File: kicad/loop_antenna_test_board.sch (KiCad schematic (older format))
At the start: 5 parts

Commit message: added board layout
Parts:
- C1, C2: footprint (none) -> loop_antenna_test_board:CAP
- C3: footprint (none) -> loop_antenna_test_board:CAP_TUNABLE
- R1: footprint (none) -> loop_antenna_test_board:RFM69W
- R2: footprint (none) -> loop_antenna_test_board:RFM69W_BB
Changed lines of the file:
@@
 LIBS:valves
 LIBS:loop_antenna_test_board
+LIBS:loop_antenna_test_board-cache
 EELAYER 25 0
 EELAYER END
@@
 F 0 "R1" H 5450 2250 60  0000 C CNN
 F 1 "RFM69W" H 5000 2950 60  0000 C CNN
-F 2 "" H 5050 3200 60  0000 C CNN
+F 2 "loop_antenna_test_board:RFM69W" H 5050 3200 60  0001 C CNN
 F 3 "" H 5050 3200 60  0000 C CNN
 	1    5000 2950
@@
 F 0 "R2" H 5450 4050 60  0000 C CNN
 F 1 "RFM69W_BB" H 5000 4750 60  0000 C CNN
-F 2 "" H 5050 5000 60  0000 C CNN
+F 2 "loop_antenna_test_board:RFM69W_BB" H 5050 5000 60  0001 C CNN
 F 3 "" H 5050 5000 60  0000 C CNN
 	1    5000 4750
@@
 F 0 "C1" H 7275 3600 50  0000 L CNN
 F 1 "C" H 7275 3400 50  0000 L CNN
-F 2 "" H 7288 3350 50  0000 C CNN
+F 2 "loop_antenna_test_board:CAP" H 7288 3350 50  0001 C CNN
 F 3 "" H 7250 3500 50  0000 C CNN
 	1    7250 3500
@@
 F 0 "C2" H 7275 4150 50  0000 L CNN
 F 1 "C" H 7275 3950 50  0000 L CNN
-F 2 "" H 7288 3900 50  0000 C CNN
+F 2 "loop_antenna_test_board:CAP" H 7288 3900 50  0001 C CNN
 F 3 "" H 7250 4050 50  0000 C CNN
 	1    7250 4050
@@
 F 0 "C3" H 7310 4520 50  0000 C CNN
 F 1 "CTRIM" H 7370 4460 50  0000 C CNN
-F 2 "" H 7250 4600 50  0000 C CNN
+F 2 "loop_antenna_test_board:CAP_TUNABLE" H 7250 4600 50  0001 C CNN
 F 3 "" H 7250 4600 50  0000 C CNN
 	1    7250 4600
@@
 	6950 3800 7250 3800
 Connection ~ 7250 3800
+Text Label 7550 3850 0    60   ~ 0
+ANTENNA
 $EndSCHEMATC

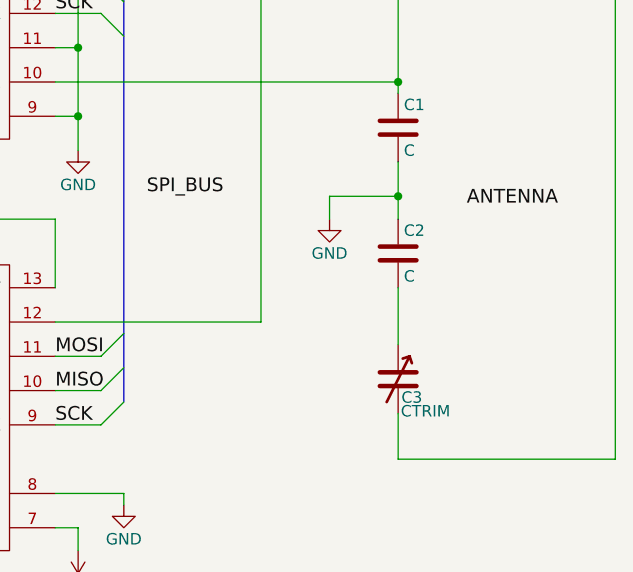
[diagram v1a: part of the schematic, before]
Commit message: switched to only having two positions for capacitors in the antenna
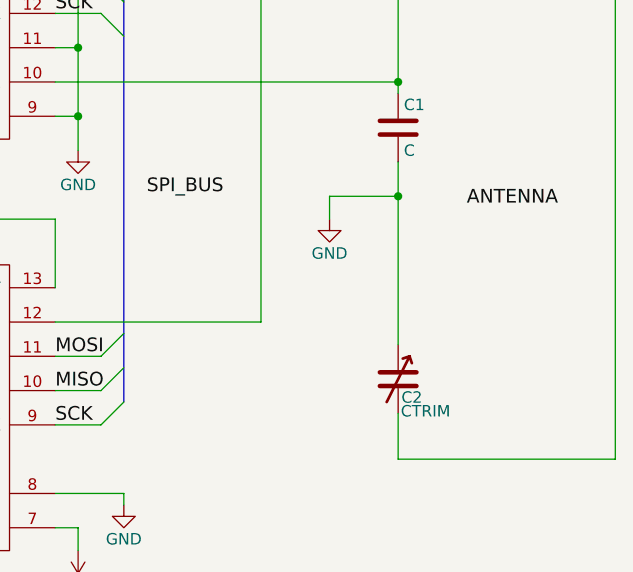
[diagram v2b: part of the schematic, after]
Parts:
- removed C2: C, loop_antenna_test_board:CAP, symbol C
- renumbered C3 to C2
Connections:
- net GND: now also C2.1
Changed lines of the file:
@@
 $EndComp
 $Comp
-L GND #PWR01
+L GND #PWR2
 U 1 1 572ED736
 P 5850 3600
-F 0 "#PWR01" H 5850 3350 50  0001 C CNN
+F 0 "#PWR2" H 5850 3350 50  0001 C CNN
 F 1 "GND" H 5850 3450 50  0000 C CNN
 F 2 "" H 5850 3600 50  0000 C CNN
@@
 	4250 5100 4050 5100
 $Comp
-L GND #PWR02
+L GND #PWR4
 U 1 1 572EDE5A
 P 6050 5150
-F 0 "#PWR02" H 6050 4900 50  0001 C CNN
+F 0 "#PWR4" H 6050 4900 50  0001 C CNN
 F 1 "GND" H 6050 5000 50  0000 C CNN
 F 2 "" H 6050 5150 50  0000 C CNN
@@
 	6050 5100 5750 5100
 $Comp
-L +3V3 #PWR03
+L +3V3 #PWR1
 U 1 1 572EDEB9
 P 4150 3550
-F 0 "#PWR03" H 4150 3400 50  0001 C CNN
+F 0 "#PWR1" H 4150 3400 50  0001 C CNN
 F 1 "+3V3" H 4150 3690 50  0000 C CNN
 F 2 "" H 4150 3550 50  0000 C CNN
@@
 	5850 5250 5750 5250
 $Comp
-L +3V3 #PWR04
+L +3V3 #PWR3
 U 1 1 572EEA16
 P 5850 5350
-F 0 "#PWR04" H 5850 5200 50  0001 C CNN
+F 0 "#PWR3" H 5850 5200 50  0001 C CNN
 F 1 "+3V3" H 5850 5490 50  0000 C CNN
 F 2 "" H 5850 5350 50  0000 C CNN
@@
 $EndComp
 $Comp
-L C C2
-U 1 1 572EEE1E
-P 7250 4050
-F 0 "C2" H 7275 4150 50  0000 L CNN
-F 1 "C" H 7275 3950 50  0000 L CNN
-F 2 "loop_antenna_test_board:CAP" H 7288 3900 50  0001 C CNN
-F 3 "" H 7250 4050 50  0000 C CNN
-	1    7250 4050
-	1    0    0    -1
-$EndComp
-$Comp
-L CTRIM C3
+L CTRIM C2
 U 1 1 572EEE5B
 P 7250 4600
-F 0 "C3" H 7310 4520 50  0000 C CNN
+F 0 "C2" H 7310 4520 50  0000 C CNN
 F 1 "CTRIM" H 7370 4460 50  0000 C CNN
 F 2 "loop_antenna_test_board:CAP_TUNABLE" H 7250 4600 50  0001 C CNN
@@
 	7250 2750 7250 3350
 Wire Wire Line
-	7250 3650 7250 3900
-Wire Wire Line
-	7250 4200 7250 4450
+	7250 3650 7250 4450
 Wire Wire Line
 	7250 4750 7250 4950
@@
 Connection ~ 7250 3300
 $Comp
-L GND #PWR05
+L GND #PWR5
 U 1 1 572EEF56
 P 6950 3900
-F 0 "#PWR05" H 6950 3650 50  0001 C CNN
+F 0 "#PWR5" H 6950 3650 50  0001 C CNN
 F 1 "GND" H 6950 3750 50  0000 C CNN
 F 2 "" H 6950 3900 50  0000 C CNN
